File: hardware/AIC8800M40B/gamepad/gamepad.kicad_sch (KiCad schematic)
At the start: 59 parts, among them J11 Conn_01x07, J12 Conn_01x10, J13 Conn_01x10, J14 Conn_01x13, J2 Rumble_TL, J3 Rumble_ML, J4 Micro_SD_Card_Det1, J5 Rumble_TR, J6 Rumble_MR, J7 Conn_01x03, J8 Conn_01x03, J8 Conn_02x15_Odd_Even, Q1 AO3402, Q2 AO3402, Q3 AO3402, Q4 AO3402, SW0 SW_Push, SW1 SW_Push, SW10 SW_Push, SW11 SW_Push, SW12 SW_Push, SW13 SW_Push, SW14 SW_Push, SW2 SW_Push, SW3 SW_Push, SW4 SW_Push, SW6 SW_Push, SW7 SW_Push, SW8 SW_Push, SW9 SW_Push, U1 PY32F002AF15P, U2 74HC165, U3 74HC165

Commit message: [hardware/aic8800m40b] update gamepad extension board
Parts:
- removed C14: 1uF, Capacitor_SMD:C_0402_1005Metric, symbol Device:C
- removed J11: Conn_01x07, Connector_PinHeader_2.54mm:PinHeader_1x07_P2.54mm_Vertical, symbol Connector_Generic:Conn_01x07
- removed J12, J13: Conn_01x10, Connector_PinHeader_2.54mm:PinHeader_1x10_P2.54mm_Vertical, symbol Connector_Generic:Conn_01x10
- removed J14: Conn_01x13, Connector_PinHeader_2.54mm:PinHeader_1x13_P2.54mm_Vertical, symbol Connector_Generic:Conn_01x13
- removed Q3: AO3402, Package_TO_SOT_SMD:SOT-23, symbol Device:Q_NMOS_GSD
- removed R18: 100, Resistor_SMD:R_0402_1005Metric, symbol Device:R
- removed R19: 1.5k, Resistor_SMD:R_0402_1005Metric, symbol Device:R
- removed R20: 100k, Resistor_SMD:R_0402_1005Metric, symbol Device:R
- removed SW0: SW_Push, LC:Key_2Pin_2.9X4.3, symbol Switch:SW_Push
- removed U1: PY32F002AF15P, Package_SO:TSSOP-20_4.4x6.5mm_P0.65mm, symbol VSF:PY32F002AF15P
- added C13: 1uF, Capacitor_SMD:C_0402_1005Metric, symbol Device:C
- added C14 (x5): 100nF, Capacitor_SMD:C_0402_1005Metric, symbol Device:C
- added D5 (x3): LED, LED_SMD:LED_0805_2012Metric, symbol Device:LED
- added J10: Conn_01x14, Connector_PinHeader_2.54mm:PinHeader_1x14_P2.54mm_Vertical, symbol Connector_Generic:Conn_01x14
- added J12: Conn_01x05, Connector_PinHeader_2.54mm:PinHeader_1x05_P2.54mm_Vertical, symbol Connector_Generic:Conn_01x05
- added J13: Conn_01x06, Connector_PinHeader_2.54mm:PinHeader_1x06_P2.54mm_Vertical, symbol Connector_Generic:Conn_01x06
- added R11 (x17): 4.7K, Resistor_SMD:R_0402_1005Metric, symbol Device:R
- added R18 (x4): 100, Resistor_SMD:R_0402_1005Metric, symbol Device:R
- added R26, R27, R28, R29, R30: 0, Resistor_SMD:R_0402_1005Metric, symbol Device:R
- added U1: 74HC595, Package_SO:SOP-16_3.9x9.9mm_P1.27mm, symbol 74xx:74HC595
- added U4: ADS7830, Package_SO:TSSOP-16_4.4x5mm_P0.65mm, symbol Analog_DAC:ADS7830
- SW1, SW10, SW12, SW13, SW14, SW2, SW3, SW4, SW6, SW7, SW8, SW9: footprint Button_Switch_THT:SW_PUSH_6mm -> Button_Switch_SMD:SW_Push_1P1T_NO_6x6mm_H9.5mm
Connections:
- net LED- is gone; now on net GND: D5.1 (K)
- net 74CLK: now also J12.5 (Pin_5), U1.11 (SRCLK)
- net 74IN: now also J12.3 (Pin_3)
- net 74PL: now also J12.4 (Pin_4), U1.12 (RCLK)
- net AD_LT: now also J10.13 (Pin_13), U4.5 (CH4)
- net AD_LX: now also J10.9 (Pin_9), U4.1 (CH0)
- net AD_LY: now also J10.10 (Pin_10), U4.2 (CH1)
- net AD_RT: now also J10.14 (Pin_14), U4.6 (CH5)
- net AD_RX: now also J10.11 (Pin_11), U4.3 (CH2)
- net AD_RY: now also J10.12 (Pin_12), U4.4 (CH3)
- net GND: now also J5.4, J6.4, C13.1, C14.1, C14.2, C14.2, C14.2, C14.2, D5.1 (K), D5.1 (K), D5.1 (K), U1.8 (GND), U4.11 (COM), U4.12 (A0), U4.13 (A1), U4.9 (GND); no longer J5.6, J6.6
- net RUMBLE_ML: now also J10.3 (Pin_3), R28.2
- net RUMBLE_MR: now also J10.4 (Pin_4), R29.2
- net RUMBLE_TL: now also J10.1 (Pin_1), R26.2
- net RUMBLE_TR: now also J10.2 (Pin_2), R27.2
- net SW_HOME: now also R11.1
- net SW_LB: now also R11.1
- net SW_LD: now also R11.1
- net SW_LL: now also R11.1
- net SW_LR: now also R11.1
- net SW_LS: now also R11.1
- net SW_LU: now also R11.1
- net SW_ML: now also R11.1
- net SW_MM: now also R11.1
- net SW_MR: now also R11.1
- net SW_RB: now also R11.1
- net SW_RD: now also R11.1
- net SW_RL: now also R11.1
- net SW_RR: now also R11.1
- net SW_RS: now also R11.1
- net SW_RU: now also R11.1
- net VCC: now also J5.6, J6.6, C13.2, C14.1, C14.1, C14.1, C14.1, C14.2, R11.2, R11.2, R11.2, R11.2, R11.2, R11.2, R11.2, R11.2, R11.2, R11.2, R11.2, R11.2, R11.2, R11.2, R11.2, R11.2, R11.2, U1.10 (~{SRCLR}), U1.16 (VCC), U4.10 (REFin/REFout), U4.16 (VDD); no longer C11.1, C12.1, C14.1, C15.1, D1.1 (K), D2.1 (K), D4.1 (K), D5.1 (K), J2.1 (Pin_1), J3.1 (Pin_1), J5.1 (Pin_1), J5.4, J6.1 (Pin_1), J6.4
- net INT: now reaches J4.1 (DAT2)
- net INT: now also J13.1 (Pin_1)
- net CS: now reaches J4.2 (DAT3/CD)
- net CS: now also J13.2 (Pin_2)
- net DI: now reaches J4.3 (CMD)
- net DI: now also J13.3 (Pin_3)
- net CLK: now reaches J4.5 (CLK)
- net CLK: now also J13.4 (Pin_4)
- net IIC_SCL renamed DO
- net DO: now also J13.6 (Pin_6), U4.14 (SCL)
- net IIC_SDA renamed SDA
- net SDA: now also J13.5 (Pin_5), U4.15 (SDA)
- net LED+: no longer names the net of D5.2 (A)
- net LED+: now also R18.2
- net USB5V_OUT renamed 5V
- net 5V: now also C11.1, C12.1, C14.1, C15.1, D1.1 (K), D2.1 (K), D4.1 (K), D5.1 (K), J2.1 (Pin_1), J3.1 (Pin_1), J5.1 (Pin_1), J6.1 (Pin_1)
- net _USB_DM renamed USB_DM
- net _USB_DP renamed USB_DP
- new net: D5.2 (A), R18.2 (x3)
- new net: R29.1, U1.3 (QD)
- new net: R28.1, U1.2 (QC)
- new net: R30.1, U1.4 (QE)
- new net: R27.1, U1.1 (QB)
- new net: R26.1, U1.15 (QA)
- new net 74OE: J12.1 (Pin_1), R11.1, U1.13 (~{OE})
- new net 74OUT: J12.2 (Pin_2), U1.14 (SER)
- new net LED0: J10.5 (Pin_5), R18.1, R30.2
- new net LED1: J10.6 (Pin_6), R18.1, U1.5 (QF)
- new net LED2: J10.7 (Pin_7), R18.1, U1.6 (QG)
- new net LED3: J10.8 (Pin_8), R18.1, U1.7 (QH)
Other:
- moved on the sheet: D5, J5, J6, J8, U2, U3

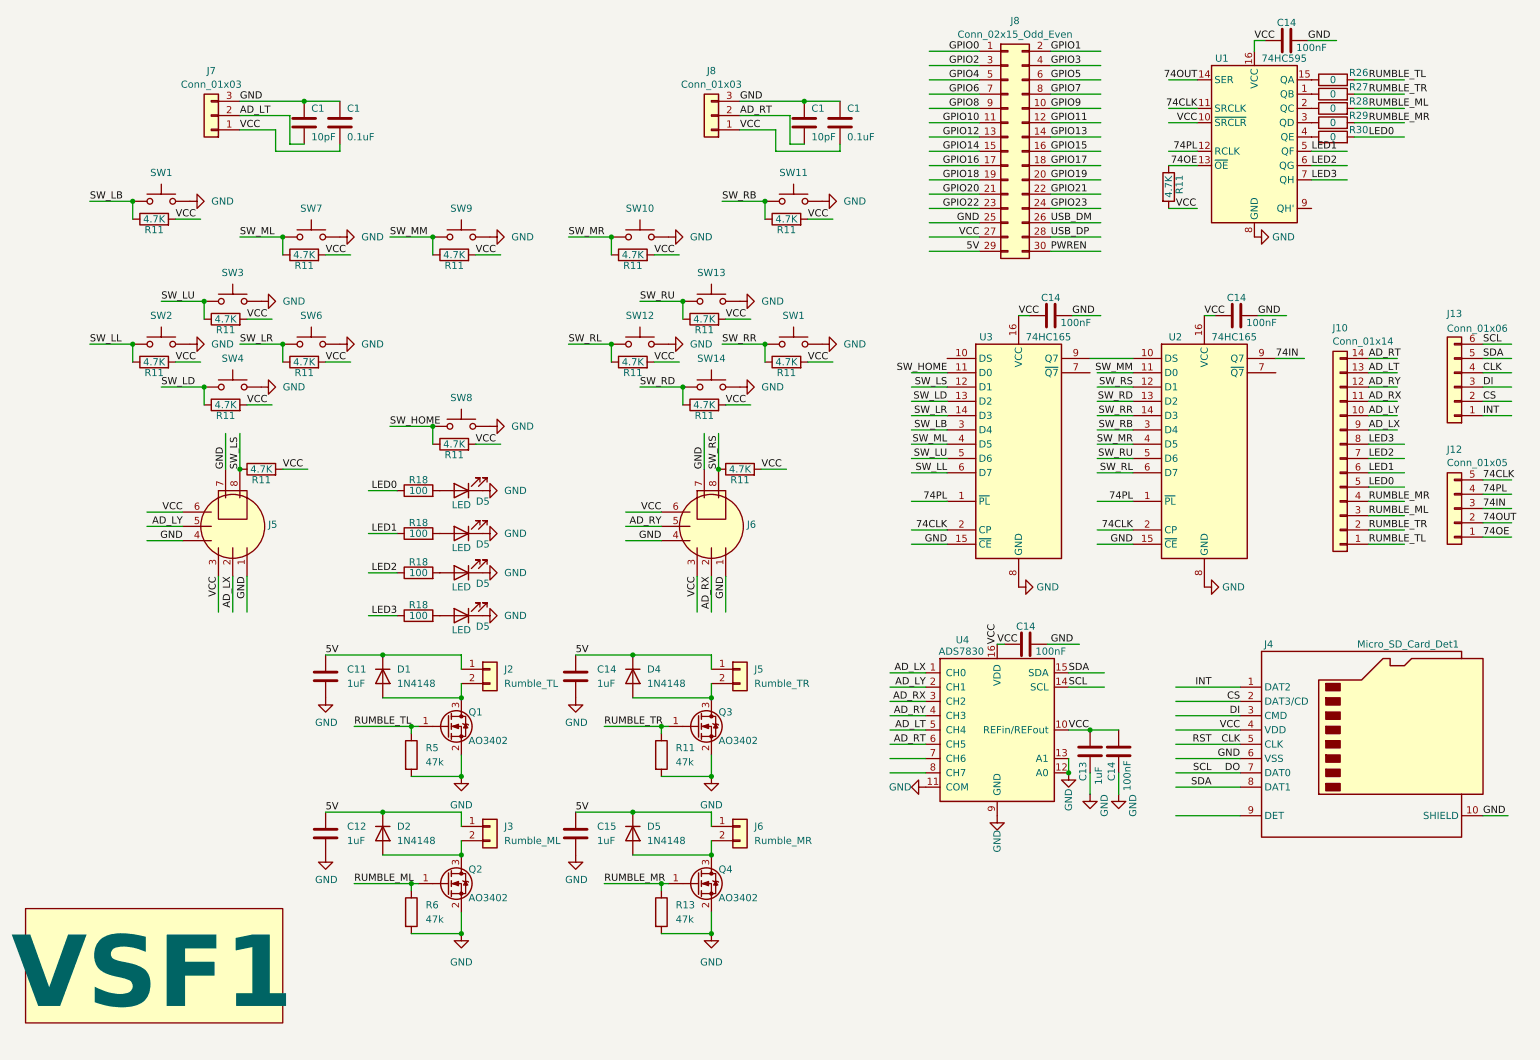
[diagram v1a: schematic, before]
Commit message: [hardware/gamepad] update pcb
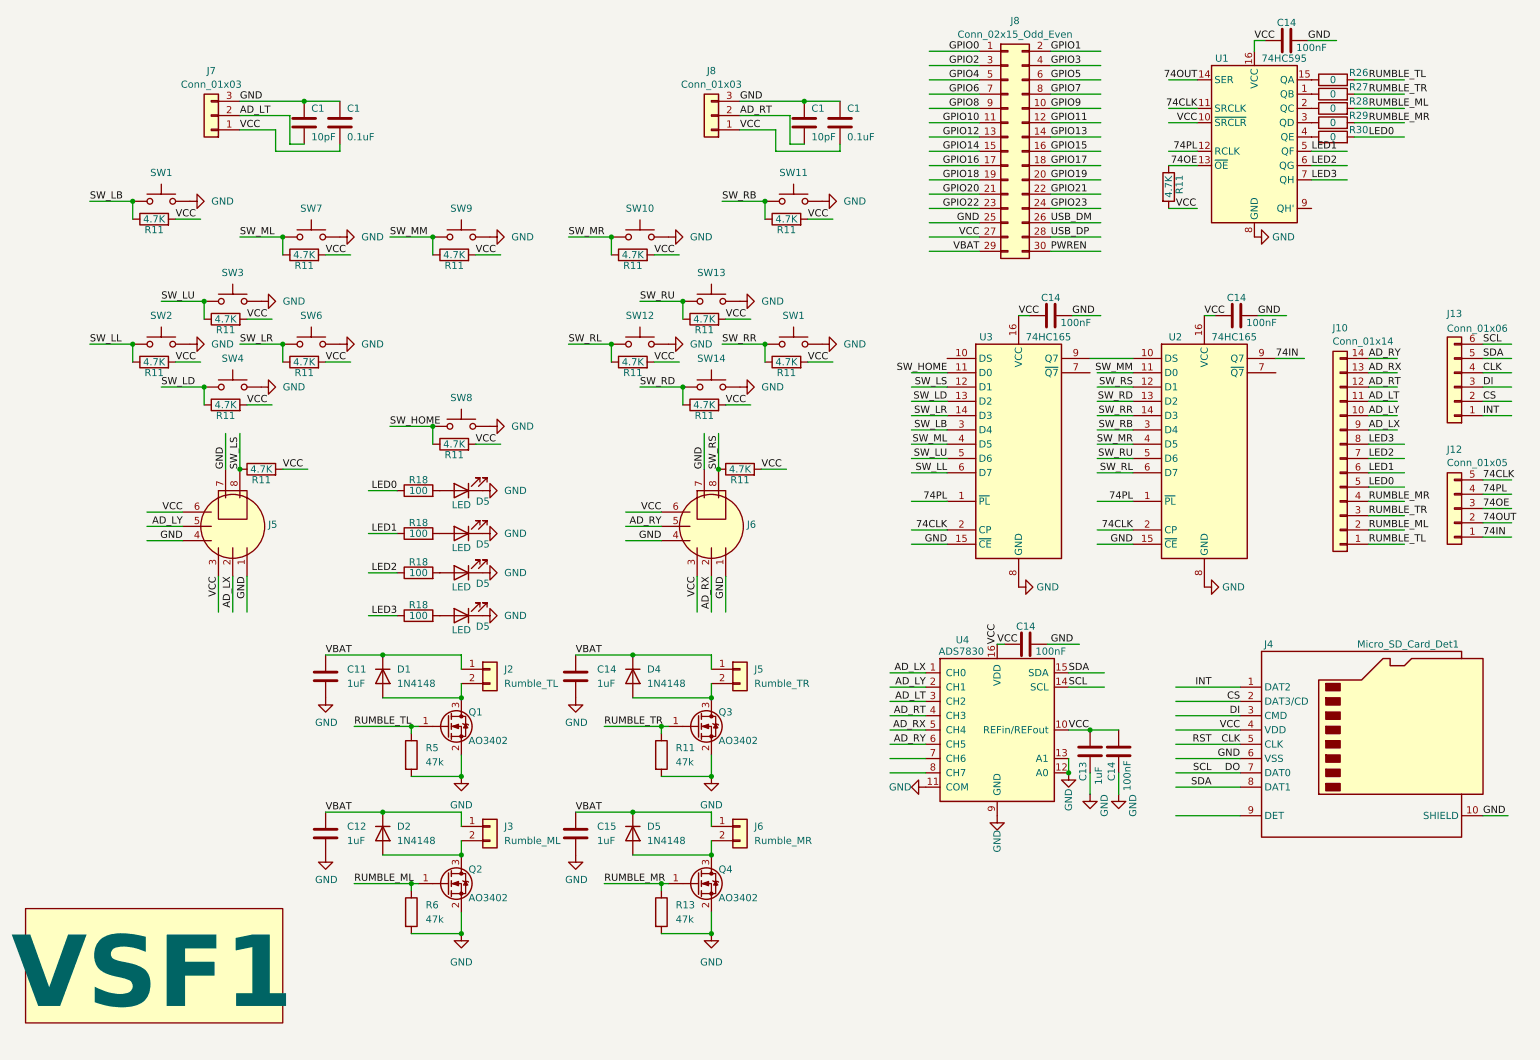
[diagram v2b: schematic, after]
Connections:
- net 74IN: now also J12.1 (Pin_1); no longer J12.3 (Pin_3)
- net 74OE: now also J12.3 (Pin_3); no longer J12.1 (Pin_1)
- net AD_LT: now also J10.11 (Pin_11), U4.3 (CH2); no longer J10.13 (Pin_13), U4.5 (CH4)
- net AD_RT: now also J10.12 (Pin_12), U4.4 (CH3); no longer J10.14 (Pin_14), U4.6 (CH5)
- net AD_RX: now also J10.13 (Pin_13), U4.5 (CH4); no longer J10.11 (Pin_11), U4.3 (CH2)
- net AD_RY: now also J10.14 (Pin_14), U4.6 (CH5); no longer J10.12 (Pin_12), U4.4 (CH3)
- net RUMBLE_ML: now also J10.2 (Pin_2); no longer J10.3 (Pin_3)
- net RUMBLE_TR: now also J10.3 (Pin_3); no longer J10.2 (Pin_2)
- net 5V renamed VBAT

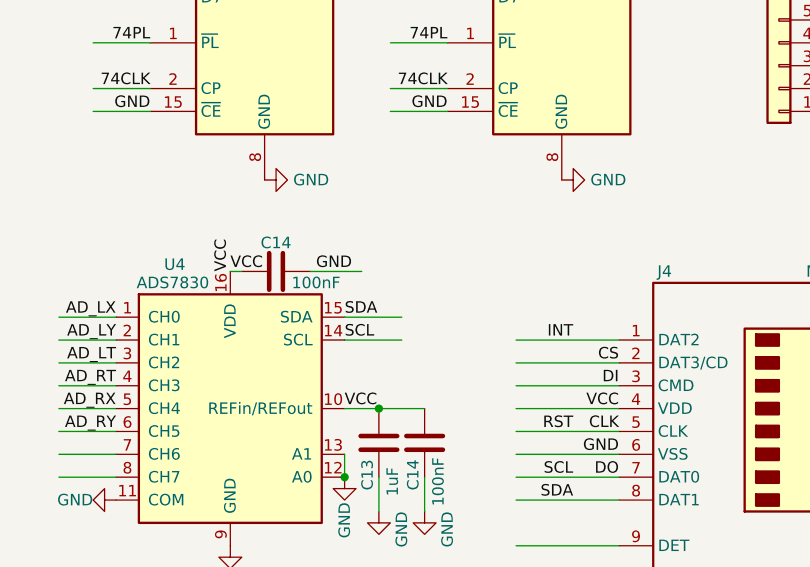
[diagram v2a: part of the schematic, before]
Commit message: [hardware/gamepad] add pull-up resister to I2C
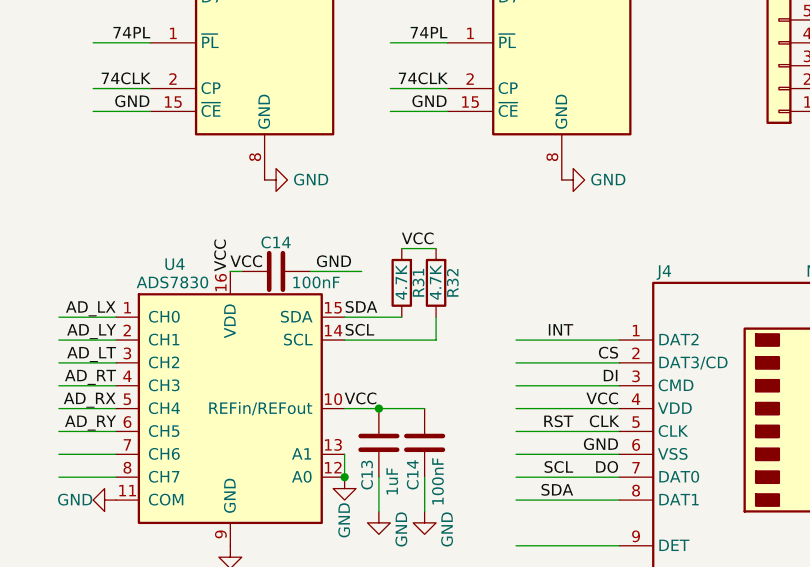
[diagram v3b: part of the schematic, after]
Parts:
- added R31, R32: 4.7K, Resistor_SMD:R_0402_1005Metric, symbol Device:R
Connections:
- net DO: now also R32.1
- net SDA: now also R31.1
- net VCC: now also R31.2, R32.2
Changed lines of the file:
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@@
 	(wire
 		(pts
-			(xy 203.2 133.35) (xy 209.55 133.35)
+			(xy 203.2 133.35) (xy 213.36 133.35)
 		)
 		(stroke
@@
 	(wire
 		(pts
+			(xy 213.36 133.35) (xy 213.36 130.81)
+		)
+		(stroke
+			(width 0)
+			(type default)
+		)
+	)
+	(wire
+		(pts
 			(xy 90.17 86.995) (xy 90.17 90.17)
 		)
@@
 	(wire
 		(pts
+			(xy 209.55 123.19) (xy 213.36 123.19)
+		)
+		(stroke
+			(width 0)
+			(type default)
+		)
+	)
+	(wire
+		(pts
 			(xy 178.435 40.64) (xy 187.325 40.64)
 		)
@@
 		)
 	)
+	(label "VCC"
+		(at 209.55 123.19 0)
+		(fields_autoplaced yes)
+		(effects
+			(font
+				(size 1.27 1.27)
+			)
+			(justify left bottom)
+		)
+	)
 	(label "CLK"
 		(at 276.86 77.47 0)
@@
 	)
 	(symbol
+		(lib_id "Device:R")
+		(at 209.55 127 180)
+		(unit 1)
+		(exclude_from_sim no)
+		(in_bom yes)
+		(on_board yes)
+		(dnp no)
+		(property "Reference" "R31"
+			(at 211.455 127 90)
+			(effects
+				(font
+					(size 1.27 1.27)
+				)
+			)
+		)
+		(property "Value" "4.7K"
+			(at 209.55 127 90)
+			(effects
+				(font
+					(size 1.27 1.27)
+				)
+			)
+		)
+		(property "Footprint" "Resistor_SMD:R_0402_1005Metric"
+			(at 211.328 127 90)
+			(effects
+				(font
+					(size 1.27 1.27)
+				)
+				(hide yes)
+			)
+		)
+		(property "Datasheet" "~"
+			(at 209.55 127 0)
+			(effects
+				(font
+					(size 1.27 1.27)
+				)
+				(hide yes)
+			)
+		)
+		(property "Description" ""
+			(at 209.55 127 0)
+			(effects
+				(font
+					(size 1.27 1.27)
+				)
+				(hide yes)
+			)
+		)
+		(pin "1"
+		)
+		(pin "2"
+		)
+		(instances
+			(project "gamepad"
+				(path "/988ff9b3-4390-4b63-b073-de63e3b1969b"
+					(reference "R31")
+					(unit 1)
+				)
+			)
+		)
+	)
+	(symbol
 		(lib_id "Connector_Generic:Conn_01x02")
 		(at 144.78 130.175 0)
@@
 					(unit 1)
 				)
+			)
+		)
+	)
+	(symbol
+		(lib_id "Device:R")
+		(at 213.36 127 180)
+		(unit 1)
+		(exclude_from_sim no)
+		(in_bom yes)
+		(on_board yes)
+		(dnp no)
+		(property "Reference" "R32"
+			(at 215.265 127 90)
+			(effects
+				(font
+					(size 1.27 1.27)
+				)
+			)
+		)
+		(property "Value" "4.7K"
+			(at 213.36 127 90)
+			(effects
+				(font
+					(size 1.27 1.27)
+				)
+			)
+		)
+		(property "Footprint" "Resistor_SMD:R_0402_1005Metric"
+			(at 215.138 127 90)
+			(effects
+				(font
+					(size 1.27 1.27)
+				)
+				(hide yes)
+			)
+		)
+		(property "Datasheet" "~"
+			(at 213.36 127 0)
+			(effects
+				(font
+					(size 1.27 1.27)
+				)
+				(hide yes)
+			)
+		)
+		(property "Description" ""
+			(at 213.36 127 0)
+			(effects
+				(font
+					(size 1.27 1.27)
+				)
+				(hide yes)
+			)
+		)
+		(pin "1"
+		)
+		(pin "2"
+		)
+		(instances
+			(project "gamepad"
+				(path "/988ff9b3-4390-4b63-b073-de63e3b1969b"
+					(reference "R32")
+					(unit 1)
+				)

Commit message: {hardware/gamepad] update
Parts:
- added C15, C16, C17, C18: 0.1uF, Capacitor_SMD:C_0402_1005Metric, symbol Device:C
- added R33, R34, R35, R36, R37, R38: 2K, Resistor_SMD:R_0402_1005Metric, symbol Device:R
- C1: value 10pF -> 0.1nF
- C1: value 10pF -> 0.1uF
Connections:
- net AD_LX: now also C16.2
- net AD_LY: now also C15.2
- net AD_RX: now also C18.2
- net AD_RY: now also C17.2
- net GND: now also C15.1, C16.1, C17.1, C18.1
- net VCC: now also R33.1, R34.1, R35.1, R36.1, R37.2, R38.2; no longer J5.3, J5.6, J6.3, J6.6, J7.1 (Pin_1), J8.1 (Pin_1)
- new net: J6.6, R35.2
- new net: J5.6, R33.2
- new net: J8.1 (Pin_1), R38.1
- new net: J6.3, R36.2
- new net: J7.1 (Pin_1), R37.1
- new net: J5.3, R34.2
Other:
- moved on the sheet: C11, C12, C14, C15, D1, D2, D4, D5, J2, J3, J5, J6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
